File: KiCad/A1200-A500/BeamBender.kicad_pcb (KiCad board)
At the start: 4 copper layers, 50 x 100 mm, 100 parts, among them J1 4-1734742-0, J2 HDMI_A_1.4, J3 STX-3501-3N, J4 Phoenix_Contact, J5 Conn_01x01, J6 Conn_02x06_Odd_Even, U1 LM1117-3.3, U2 GW1NR-UV9LQ144P, U3 ADV7513BSWZ, U4 MCP1702T-1802E_CB, U5 AK5720VT, X1 Abracon ASE-27.000MHZ-L-R-T, X2 Oscillator_7.0x5.0mm, X3 5.0x3.2mm

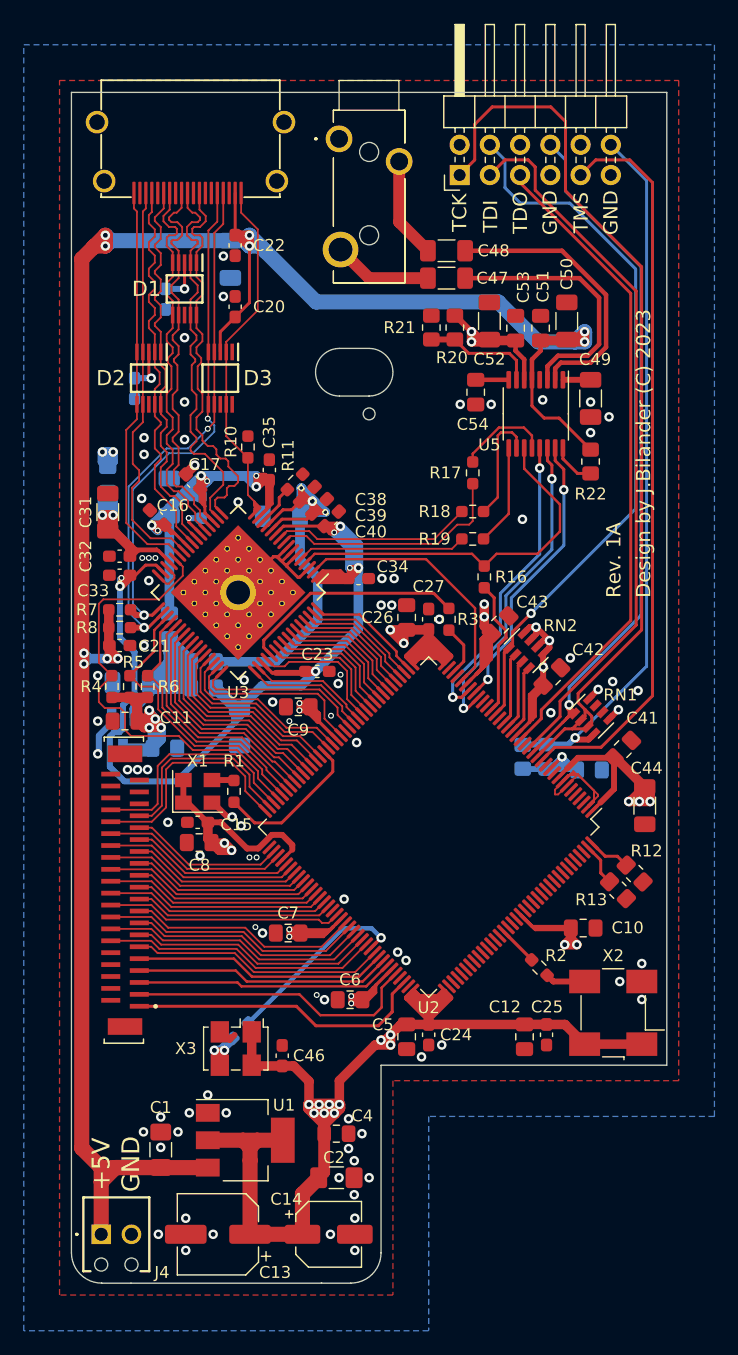
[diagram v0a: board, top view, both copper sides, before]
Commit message: Fixed assignment/enumeration of all capacitors from C1 to C54
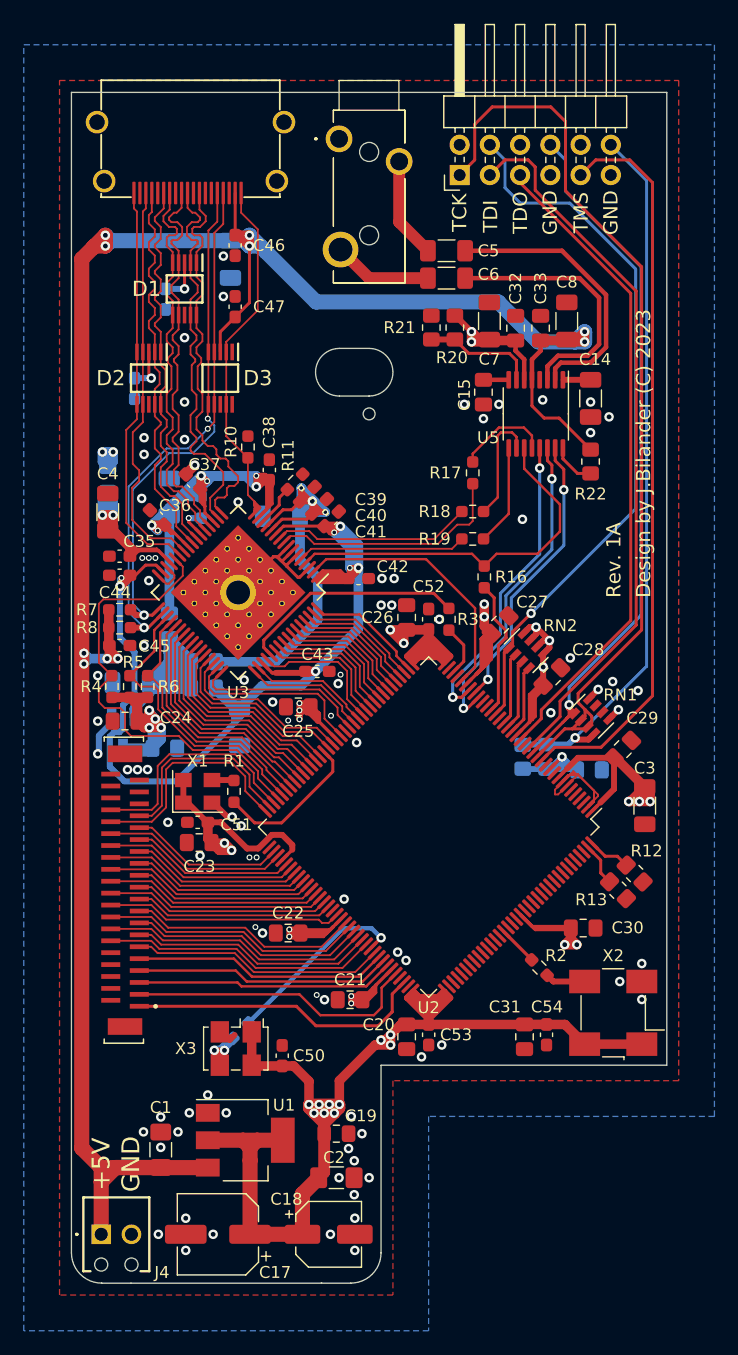
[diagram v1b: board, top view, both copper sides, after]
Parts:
- removed the C3 at (111.5, 54.2)
- removed the C4 at (120.4, 127.7)
- removed the C47 at (129.6, 55.8)
- removed the C49 at (141.7, 65.9)
- removed the C5 at (126.3, 119.5)
- removed the C51 at (137.5, 60.0)
- added C13: 10uF (1206), Capacitor_SMD:C_1206_3216Metric_Pad1.33x1.80mm_HandSolder, B.Cu at (111.5, 54.2)
- added C14: 0.47uF (1206), Capacitor_SMD:C_1206_3216Metric_Pad1.33x1.80mm_HandSolder, F.Cu at (141.7, 65.9)
- added C19: 0.1uF (0805), Capacitor_SMD:C_0805_2012Metric_Pad1.15x1.40mm_HandSolder, F.Cu at (120.4, 127.7)
- added C20: 0.1uF, Capacitor_SMD:C_0805_2012Metric_Pad1.18x1.45mm_HandSolder, F.Cu at (126.3, 119.5)
- added C33: 0.1uF (0805), Capacitor_SMD:C_0805_2012Metric_Pad1.18x1.45mm_HandSolder, F.Cu at (137.5, 60.0)
- added C6: 10uF (1206), Capacitor_SMD:C_1206_3216Metric_Pad1.33x1.80mm_HandSolder, F.Cu at (129.6, 55.8)
- C3: renamed from C44; value 10uF (1206) -> 10uF
- C34: renamed from C45; value 100nF (0805) -> 0.1uF (0805)
- C35: renamed from C32; value 0.1uF (0603) -> 0.1uF
- C36: renamed from C16; value 0.1uF (0603) -> 0.1uF
- C37: renamed from C17; value 0.1uF (0603) -> 0.1uF
- C38: renamed from C35; value 0.1uF (0603) -> 0.1uF
- C39: renamed from C38; value 0.1uF (0603) -> 0.1uF
- C40: renamed from C39; value 0.1uF (0603) -> 0.1uF
- C41: renamed from C40; value 0.1uF (0603) -> 0.1uF
- C42: renamed from C34; value 0.1uF (0603) -> 0.1uF
- C43: renamed from C23; value 0.1uF (0603) -> 0.1uF
- C44: renamed from C33; value 0.1uF (0603) -> 0.1uF
- moved C15 0.65 mm to (132.7, 65.4)
- renumbered C30 to C10, C37 to C11, C36 to C12, C54 to C15, C28 to C16, C13 to C17, C14 to C18, C6 to C21, C7 to C22, C8 to C23, C11 to C24, C9 to C25, C43 to C27, C42 to C28, C41 to C29, C10 to C30, C12 to C31, C53 to C32, C31 to C4, C21 to C45, C22 to C46, C20 to C47, C19 to C48, C18 to C49, C48 to C5, C46 to C50, C15 to C51, C27 to C52, C24 to C53, C25 to C54, C52 to C7, C50 to C8, C29 to C9
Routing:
- net 3V3: track 318.2 -> 319.9 mm
- net /BeamBender_FPGA/REGO: track 2.78 -> 2.12 mm
- net GND: vias 82 -> 84

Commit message: Some silkscreen text fixes and OSHW-logos placement done
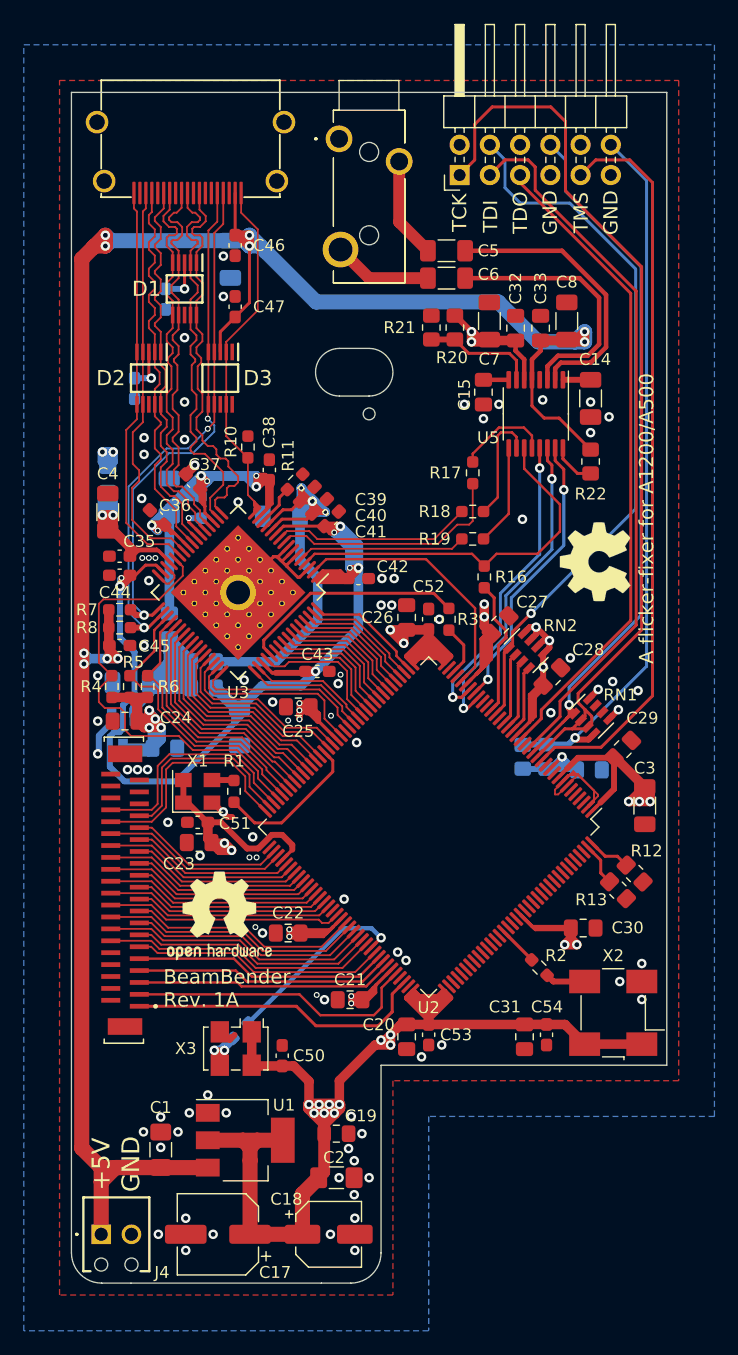
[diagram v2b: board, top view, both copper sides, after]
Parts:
- added REF**: OSHW-Logo2_9.8x8mm_SilkScreen, Symbol:OSHW-Logo2_9.8x8mm_SilkScreen, F.Cu at (110.5, 109.4)
- added REF**: OSHW-Symbol_6.7x6mm_SilkScreen, Symbol:OSHW-Symbol_6.7x6mm_SilkScreen, F.Cu at (142.1, 79.6)
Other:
- board text added: "A flicker-fixer for A1200/A500"
- board text added: "BeamBender Rev. 1A"
- board text added: "Design by J.Bilander (C) 2023, 2024"
- board text removed: "Design by J.Bilander (C) 2023"
- board text removed: "Rev. 1A"

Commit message: Fixed enumeration/order of all resistors on board and their reference placement on silkscreen
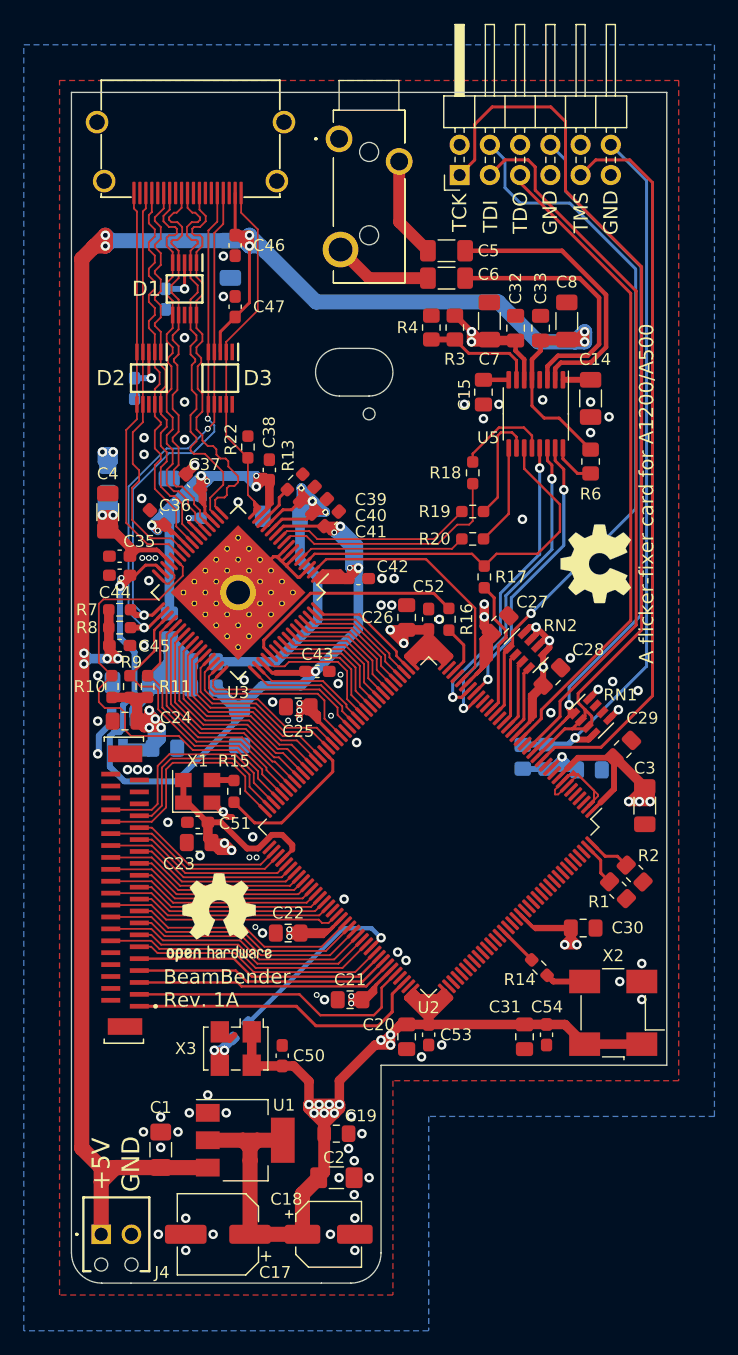
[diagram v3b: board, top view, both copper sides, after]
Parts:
- moved REF** 0.18 mm to (142.2, 79.8)
- moved REF** 0.15 mm to (110.5, 109.5)
- renumbered R13 to R1, R4 to R10, R6 to R11, R9 to R12, R11 to R13, R2 to R14, R1 to R15, R3 to R16, R16 to R17, R17 to R18, R18 to R19, R12 to R2, R19 to R20, R15 to R21, R10 to R22, R20 to R3, R21 to R4, R14 to R5, R22 to R6, R5 to R9
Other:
- board text added: "A flicker-fixer card for A1200/A500"
- board text removed: "A flicker-fixer for A1200/A500"

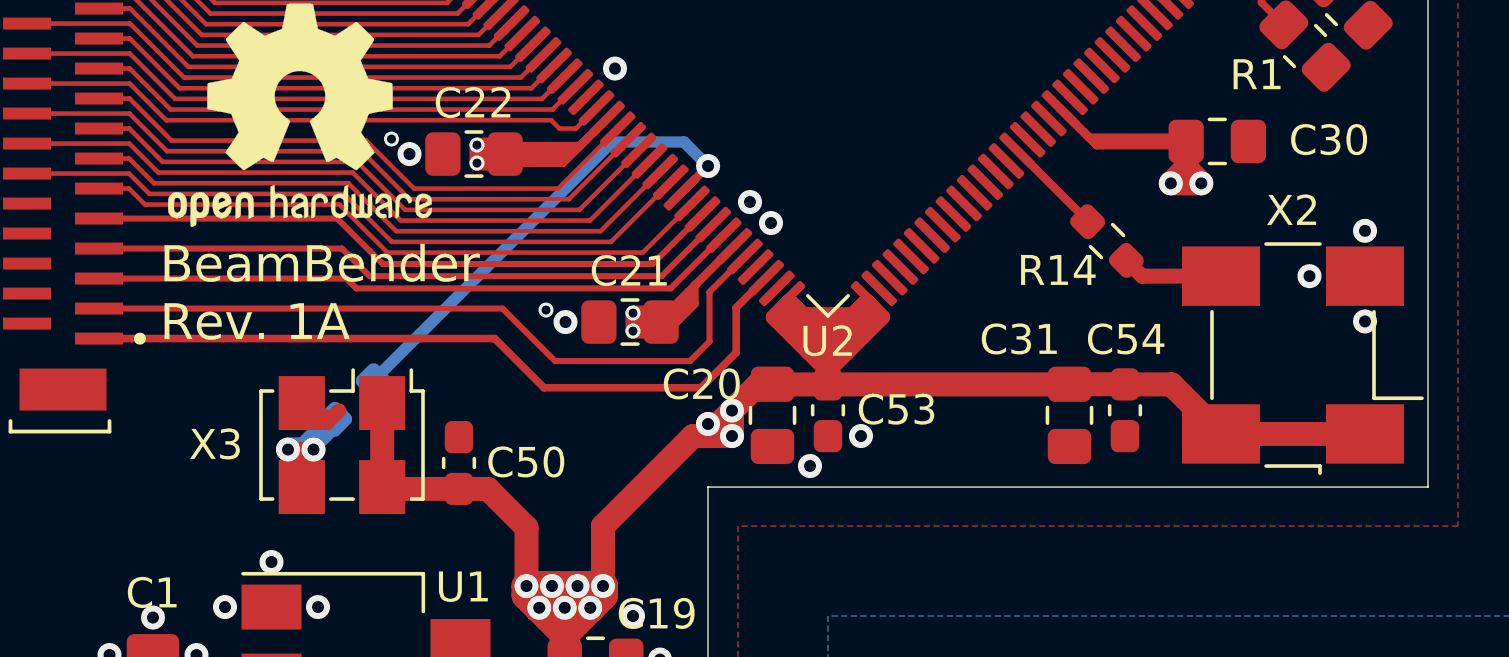
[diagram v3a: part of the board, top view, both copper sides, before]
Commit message: Fixed ordering of L1-L4, changed R14-R21 to 33 Ohms, and swapped X2 and X3 reference
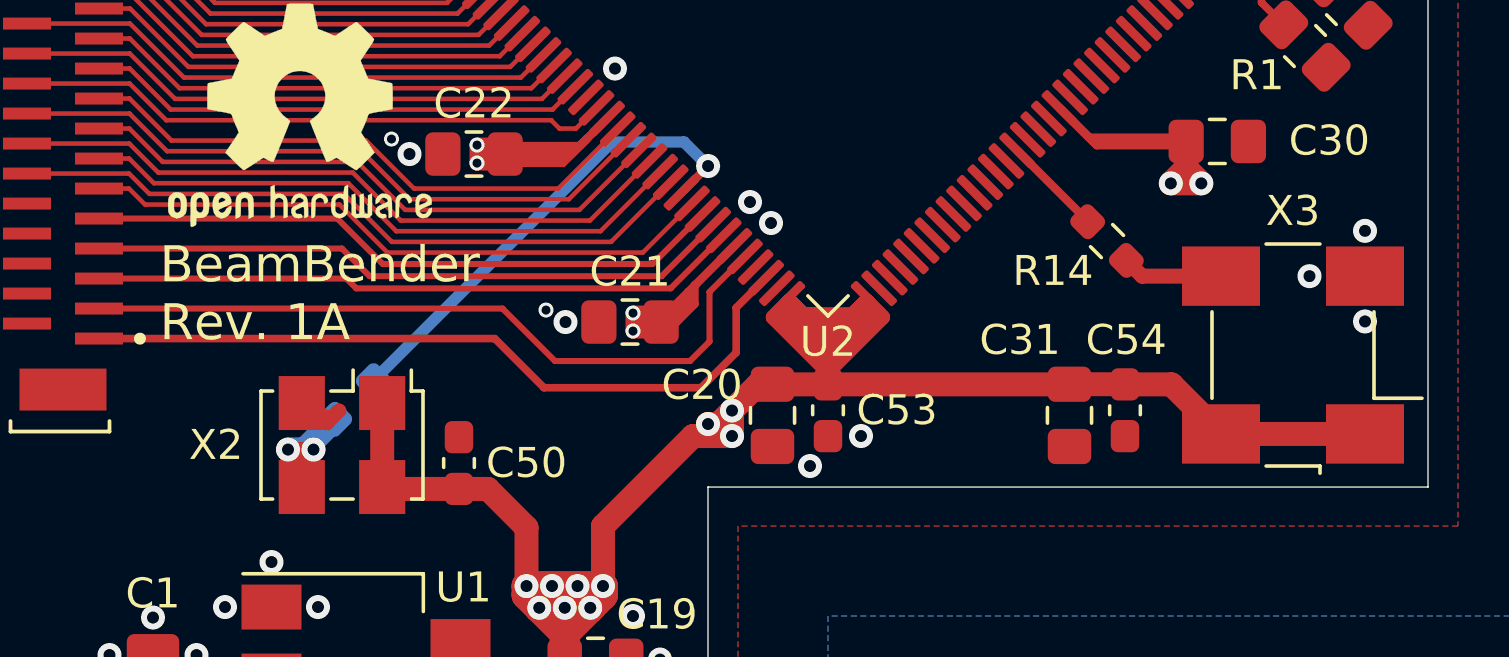
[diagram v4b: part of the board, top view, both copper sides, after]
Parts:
- R14, R15, R16, R17, R18, R19, R20, R21: value 22 -> 33
- renumbered L2 to L1, L4 to L2, L1 to L4, X3 to X2, X2 to X3
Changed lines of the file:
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@@
       (effects (font (size 1 1) (thickness 0.15)))
     )
-    (fp_text value 22 (at 0 1.43) (layer F.Fab) hide
+    (fp_text value 33 (at 0 1.43) (layer F.Fab) hide
       (effects (font (size 1 1) (thickness 0.15)))
     )
@@
       (effects (font (size 1 1) (thickness 0.15)))
     )
-    (fp_text value 22 (at 0 1.43) (layer F.Fab) hide
+    (fp_text value 33 (at 0 1.43) (layer F.Fab) hide
       (effects (font (size 1 1) (thickness 0.15)))
     )
@@
       (effects (font (size 1 1) (thickness 0.15)))
     )
-    (fp_text value 22 (at 0 1.43 90) (layer F.Fab) hide
+    (fp_text value 33 (at 0 1.43 90) (layer F.Fab) hide
       (effects (font (size 1 1) (thickness 0.15)))
     )
@@
       (effects (font (size 1 1) (thickness 0.15)))
     )
-    (fp_text value 22 (at 0 1.43 90) (layer F.Fab) hide
+    (fp_text value 33 (at 0 1.43 90) (layer F.Fab) hide
       (effects (font (size 1 1) (thickness 0.15)))
     )
@@
     (tags "SMD SMT crystal oscillator hand-soldering")
     (attr smd)
-    (fp_text reference X3 (at 4.2 0) (layer F.SilkS)
+    (fp_text reference X2 (at 4.2 0) (layer F.SilkS)
       (effects (font (size 1 1) (thickness 0.15)))
     )
@@
       (effects (font (size 1 1) (thickness 0.15)) (justify mirror))
     )
-    (fp_text value 22 (at 0 -1.43 225) (layer B.Fab) hide
+    (fp_text value 33 (at 0 -1.43 225) (layer B.Fab) hide
       (effects (font (size 1 1) (thickness 0.15)) (justify mirror))
     )
@@
     (tags "capacitor handsolder")
     (attr smd)
-    (fp_text reference L4 (at 0 -1.6428) (layer B.SilkS)
+    (fp_text reference L2 (at 0 -1.72) (layer B.SilkS)
       (effects (font (size 1 1) (thickness 0.15)) (justify mirror))
     )
@@
     (tags "capacitor handsolder")
     (attr smd)
-    (fp_text reference L2 (at -0.041 1.5674) (layer B.SilkS)
+    (fp_text reference L1 (at -0.04 1.655) (layer B.SilkS)
       (effects (font (size 1 1) (thickness 0.15)) (justify mirror))
     )
@@
     (tags "capacitor handsolder")
     (attr smd)
-    (fp_text reference L1 (at 0 1.68) (layer B.SilkS)
+    (fp_text reference L4 (at 0 1.825) (layer B.SilkS)
       (effects (font (size 1 1) (thickness 0.15)) (justify mirror))
     )
@@
       (effects (font (size 1 1) (thickness 0.15)))
     )
-    (fp_text value 22 (at 0 1.43 90) (layer F.Fab) hide
+    (fp_text value 33 (at 0 1.43 90) (layer F.Fab) hide
       (effects (font (size 1 1) (thickness 0.15)))
     )
@@
     (tags "SMD SMT crystal oscillator hand-soldering")
     (attr smd)
-    (fp_text reference X2 (at 4.8 0) (layer F.SilkS)
+    (fp_text reference X3 (at 4.8 0) (layer F.SilkS)
       (effects (font (size 1 1) (thickness 0.15)))
     )
@@
     (tags "resistor handsolder")
     (attr smd)
-    (fp_text reference R14 (at 0.459619 -1.873833 180) (layer F.SilkS)
+    (fp_text reference R14 (at 0.565685 -1.979899 180) (layer F.SilkS)
       (effects (font (size 1 1) (thickness 0.15)))
     )
-    (fp_text value 22 (at 0 1.43 135) (layer F.Fab) hide
+    (fp_text value 33 (at 0 1.43 135) (layer F.Fab) hide
       (effects (font (size 1 1) (thickness 0.15)))
     )
@@
       (effects (font (size 1 1) (thickness 0.15)))
     )
-    (fp_text value 22 (at 0 1.43 90) (layer F.Fab) hide
+    (fp_text value 33 (at 0 1.43 90) (layer F.Fab) hide
       (effects (font (size 1 1) (thickness 0.15)))
     )
@@
   (segment (start 111.7235 97.967) (end 111.761 98.0045) (width 0.5) (layer F.Cu) (net 152))
   (segment (start 109.911 97.967) (end 111.7235 97.967) (width 0.5) (layer F.Cu) (net 152))
-  (via (at 110.111 120.667) (size 0.8) (drill 0.4) (layers F.Cu B.Cu) (net 169))
-  (via (at 110.961 120.667) (size 0.8) (drill 0.4) (layers F.Cu B.Cu) (net 169))
-  (segment (start 110.111 121.457) (end 110.571 121.917) (width 0.5) (layer F.Cu) (net 169))
-  (segment (start 110.111 120.667) (end 110.111 121.457) (width 0.5) (layer F.Cu) (net 169))
-  (segment (start 110.961 121.527) (end 110.571 121.917) (width 0.5) (layer F.Cu) (net 169))
-  (segment (start 110.961 120.667) (end 110.961 121.527) (width 0.5) (layer F.Cu) (net 169))
-  (segment (start 110.111 120.667) (end 110.961 120.667) (width 0.5) (layer F.Cu) (net 169))
-  (segment (start 110.111 120.667) (end 110.261 120.667) (width 0.5) (layer F.Cu) (net 169))
-  (segment (start 110.571 120.977) (end 110.571 121.917) (width 0.5) (layer F.Cu) (net 169))
-  (segment (start 110.261 120.667) (end 110.571 120.977) (width 0.5) (layer F.Cu) (net 169))
-  (segment (start 110.711 120.617) (end 110.711 120.667) (width 0.8) (layer B.Cu) (net 169))
-  (segment (start 111.665765 119.662235) (end 110.711 120.617) (width 0.8) (layer B.Cu) (net 169))
-  (segment (start 110.711 120.667) (end 110.961 120.667) (width 0.8) (layer B.Cu) (net 169))
-  (segment (start 110.111 120.667) (end 110.711 120.667) (width 0.8) (layer B.Cu) (net 169))
   (segment (start 139.386 64.3545) (end 139.5735 64.3545) (width 0.381) (layer F.Cu) (net 153))
   (segment (start 141.711 64.3545) (end 139.5735 64.3545) (width 0.5) (layer F.Cu) (net 153))
@@
   (segment (start 133.611 82.6512) (end 132.782 81.8222) (width 0.254) (layer F.Cu) (net 168))
   (segment (start 133.611 84.417) (end 133.611 82.6512) (width 0.254) (layer F.Cu) (net 168))
+  (via (at 110.111 120.667) (size 0.8) (drill 0.4) (layers F.Cu B.Cu) (net 169))
+  (via (at 110.961 120.667) (size 0.8) (drill 0.4) (layers F.Cu B.Cu) (net 169))
+  (segment (start 110.111 121.457) (end 110.571 121.917) (width 0.5) (layer F.Cu) (net 169))
+  (segment (start 110.111 120.667) (end 110.111 121.457) (width 0.5) (layer F.Cu) (net 169))
+  (segment (start 110.961 121.527) (end 110.571 121.917) (width 0.5) (layer F.Cu) (net 169))
+  (segment (start 110.961 120.667) (end 110.961 121.527) (width 0.5) (layer F.Cu) (net 169))
+  (segment (start 110.111 120.667) (end 110.961 120.667) (width 0.5) (layer F.Cu) (net 169))
+  (segment (start 110.111 120.667) (end 110.261 120.667) (width 0.5) (layer F.Cu) (net 169))
+  (segment (start 110.571 120.977) (end 110.571 121.917) (width 0.5) (layer F.Cu) (net 169))
+  (segment (start 110.261 120.667) (end 110.571 120.977) (width 0.5) (layer F.Cu) (net 169))
+  (segment (start 110.711 120.617) (end 110.711 120.667) (width 0.8) (layer B.Cu) (net 169))
+  (segment (start 111.665765 119.662235) (end 110.711 120.617) (width 0.8) (layer B.Cu) (net 169))
+  (segment (start 110.711 120.667) (end 110.961 120.667) (width 0.8) (layer B.Cu) (net 169))
+  (segment (start 110.111 120.667) (end 110.711 120.667) (width 0.8) (layer B.Cu) (net 169))
   (zone (net 1) (net_name GND) (layer F.Cu) (hatch edge 0.508)
     (connect_pads (clearance 0.2032))
